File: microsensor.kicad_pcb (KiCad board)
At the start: 4 copper layers, 27 x 26 mm, 24 parts, among them J1 ARM SWD, Q1 IRLML2244TRPBF, SW1 Control, U1 HDC2080, U2 RV-3028-C7, U3 NORA B206, Y1 32768

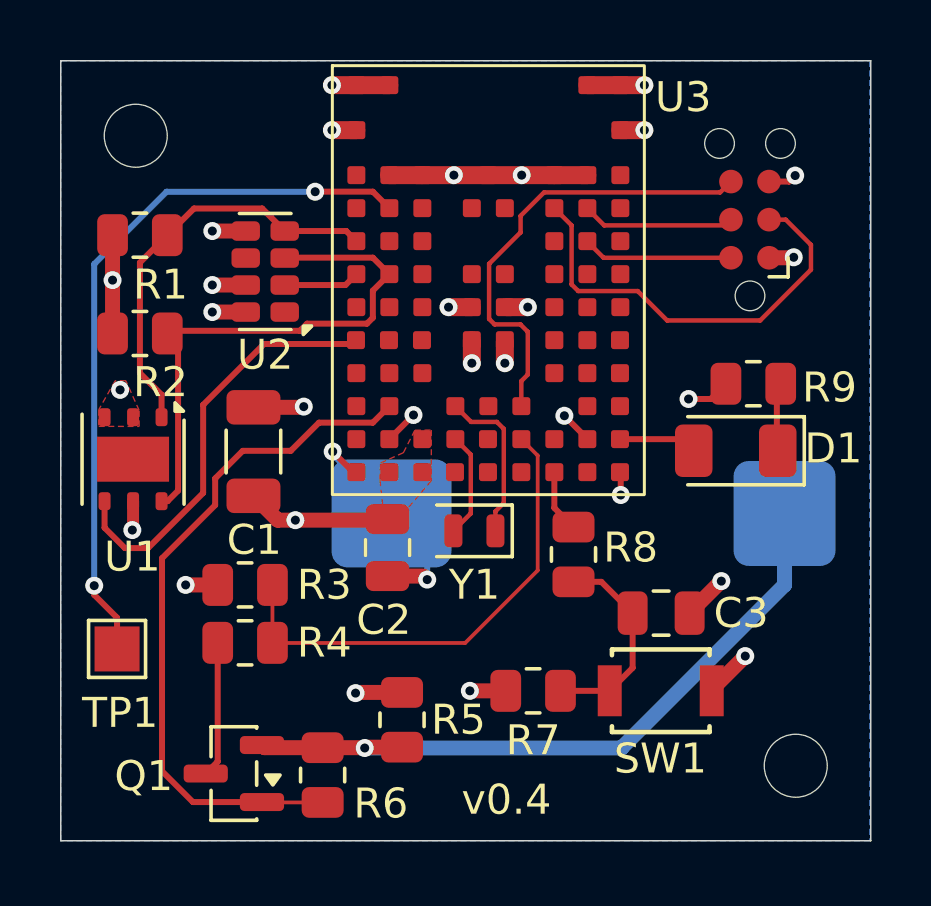
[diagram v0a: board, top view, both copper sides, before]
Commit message: Remove RV3028 (firmware will use GRTC)
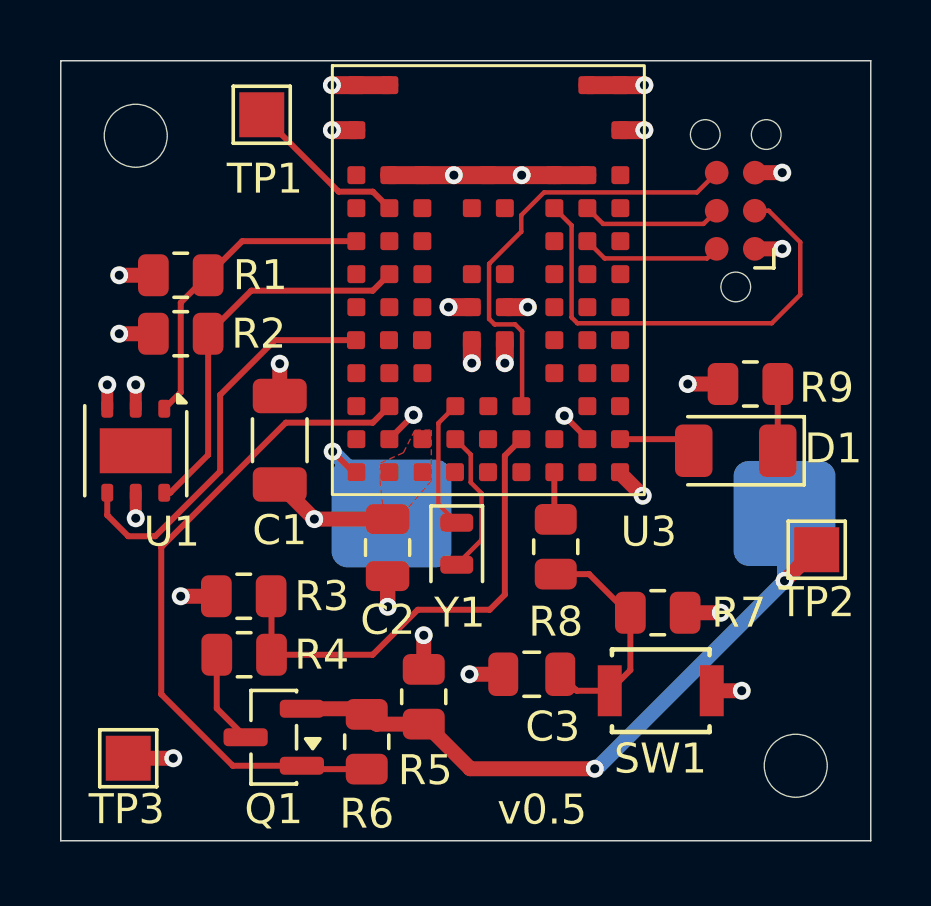
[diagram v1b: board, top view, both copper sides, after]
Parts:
- removed U2: RV-3028-C7, Package_SON:MicroCrystal_C7_SON-8_1.5x3.2mm_P0.9mm
- added TP2: P1.13, TestPoint:TestPoint_Pad_1.5x1.5mm, F.Cu at (55.2, 46.3)
- added TP3: P1.13, TestPoint:TestPoint_Pad_1.5x1.5mm, F.Cu at (32.2, 53.2)
- BT0: value CR1225 -> CR2032
- C2: value 100n -> 0.1u
- C3: value 100nF -> 0.1u
- moved TP1 18.4 mm to (36.7, 31.8)
- moved R7 4.90 mm to (49.9, 48.4), turned to 0 degrees
- moved C3 4.77 mm to (45.7, 50.5), turned to 180 degrees
- moved R1 1.91 mm to (34.0, 37.1)
- moved R6 1.84 mm to (40.2, 52.7)
- moved Q1 1.80 mm to (37.1, 52.5)
- moved R2 1.36 mm to (34.0, 39.1)
- moved R5 1.06 mm to (42.1, 51.2)
- moved C1 0.95 mm to (37.3, 42.6)
- moved Y1 0.73 mm to (43.2, 46.1), turned to -90 degrees
- moved R8 0.64 mm to (46.5, 46.2)
- moved J1 0.56 mm to (52.5, 35.0)
- moved R4 0.40 mm to (36.1, 49.8)
- moved R3 0.38 mm to (36.1, 47.9)
- moved U1 0.30 mm to (32.5, 43.0)
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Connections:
- U3 pad G9: /~{RTCINT} -> unconnected-(U3C-P1.05-PadG9)
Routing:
- net Net-(TP1-Pad1): track 24.2 -> 5.54 mm, vias 2 -> 0
- net /SCL: track 17.9 -> 12.9 mm
- net /SDA: track 13.9 -> 10.5 mm
- net +3V3: track 13.7 -> 10.4 mm
- net /~{RTCINT}: track 2.54 -> 0.00 mm
- net /XL1: track 3.51 -> 4.89 mm
- net Net-(Q1-D): track 4.52 -> 3.15 mm
- net /~{RESET}: track 14.5 -> 15.7 mm
- net /XL2: track 5.44 -> 4.37 mm
- net GND: track 34.7 -> 35.7 mm
- net /VSENSE EN: track 23.1 -> 22.2 mm
- net Net-(C3-Pad1): track 6.95 -> 7.70 mm
- net /SWO: track 15.4 -> 14.7 mm
- net /~{SWPUSH}: track 2.10 -> 1.53 mm
- net +BATT: track 23.3 -> 22.9 mm, vias 1 -> 2
- removed copper zone on B.Cu, net GND
- removed copper zone on F.Cu, net GND
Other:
- board text added: "v0.5"
- board text removed: "v0.4"

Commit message: Put TP together, minor refactors, added more dimensions
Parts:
- TP1: value P1.13 -> GND
- TP2: value P1.13 -> BAT
- TP3: value P1.13 -> TX
- moved TP2 24.4 mm to (31.3, 51.0)
- moved TP1 22.9 mm to (31.3, 54.0)
- moved TP3 5.41 mm to (31.3, 47.9)
- moved R9 3.42 mm to (52.6, 44.2)
- moved R7 2.90 mm to (47.9, 46.3), turned to 90 degrees
- moved D1 1.12 mm to (52.0, 42.0)
- moved R8 0.56 mm to (46.0, 46.3)
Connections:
- TP1 pad 1: Net-(TP1-Pad1) -> GND
- TP3 pad 1: GND -> /TX
- U3 pad J8: Net-(TP1-Pad1) -> /TX
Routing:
- net /TX: track 0.00 -> 22.6 mm
- net +BATT: track 22.9 -> 35.7 mm, vias 2 -> 1
- net Net-(TP1-Pad1): track 5.54 -> 0.00 mm
- net /VSENSE EN: track 22.2 -> 18.5 mm
- net /LED: track 2.87 -> 2.21 mm

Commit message: minor re-routing
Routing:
- net /SWO: track 14.7 -> 23.8 mm
- net GND: track 35.7 -> 43.8 mm, vias 24 -> 27

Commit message: add solder mask expansion (0.051)
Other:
- rule pad_to_mask_clearance: 0 -> 0.051
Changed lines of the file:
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@@
 			(dielectric_constraints no)
 		)
-		(pad_to_mask_clearance 0)
+		(pad_to_mask_clearance 0.051)
 		(allow_soldermask_bridges_in_footprints no)
 		(tenting
@@
 		(capping no)
 		(filling no)
+		(zone_defaults)
 		(pcbplotparams
 			(layerselection 0x00000000_00000000_55555555_5755f5ff)
